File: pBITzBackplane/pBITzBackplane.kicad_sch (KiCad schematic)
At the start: 13 parts

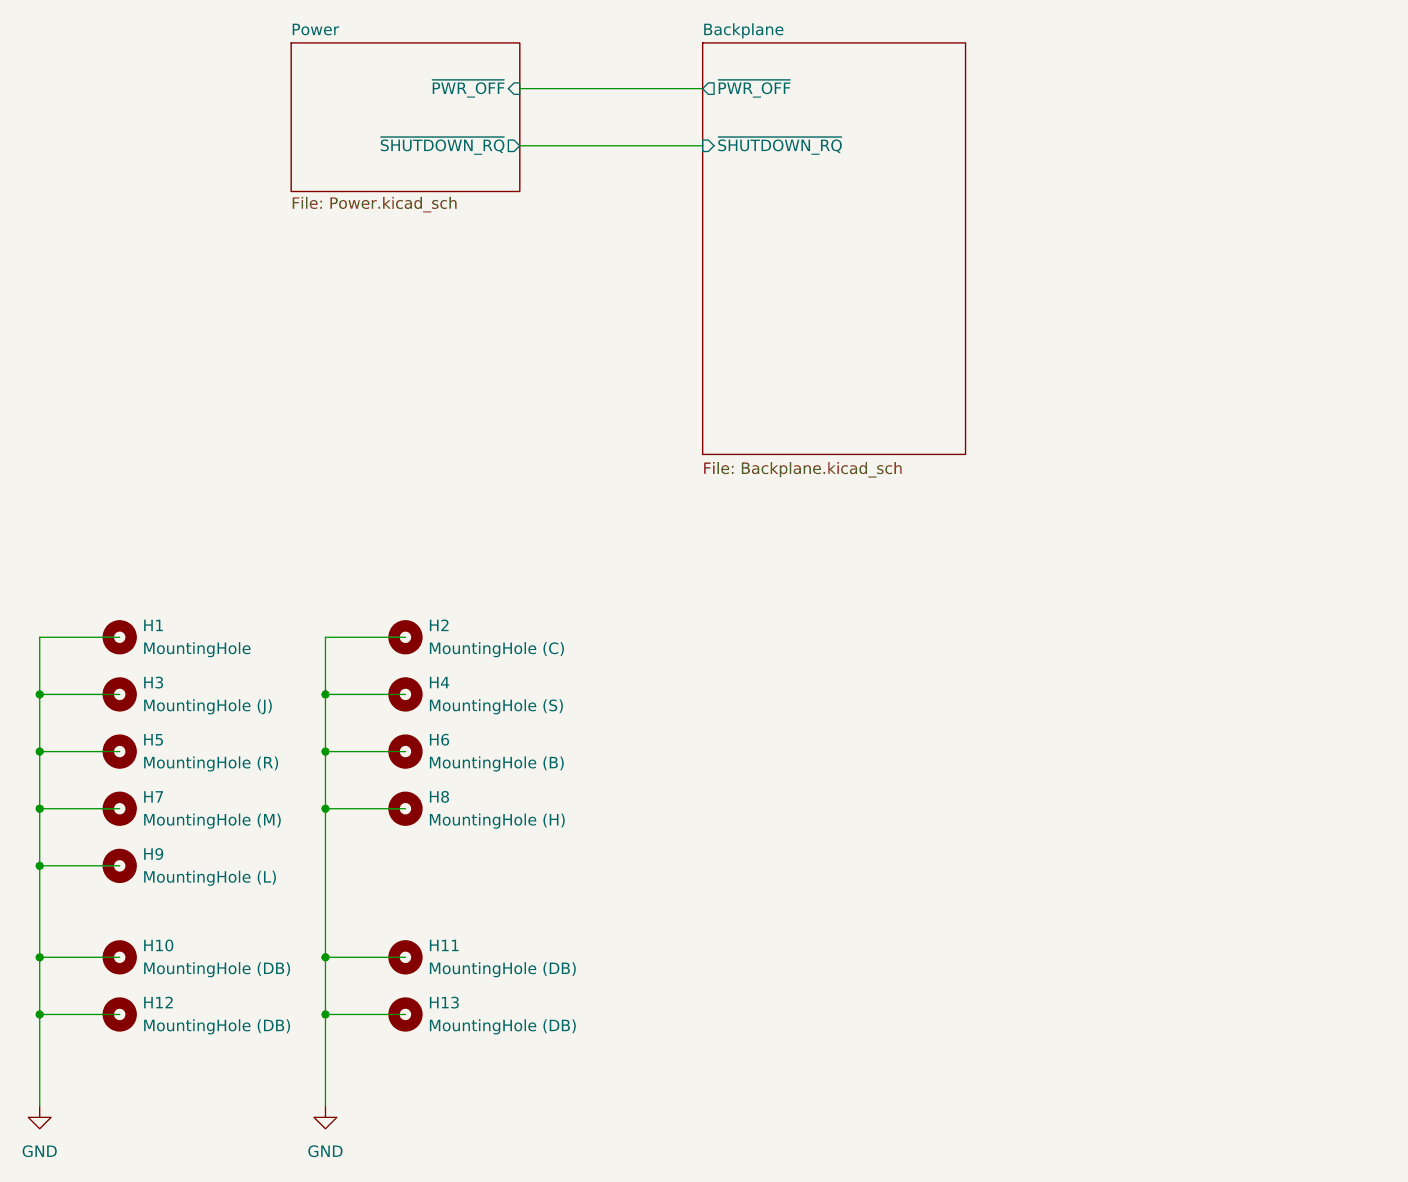
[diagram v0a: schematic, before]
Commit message: Changed the pBITz backplane connector from a PCIe 8x to a DIN 41612 connector.
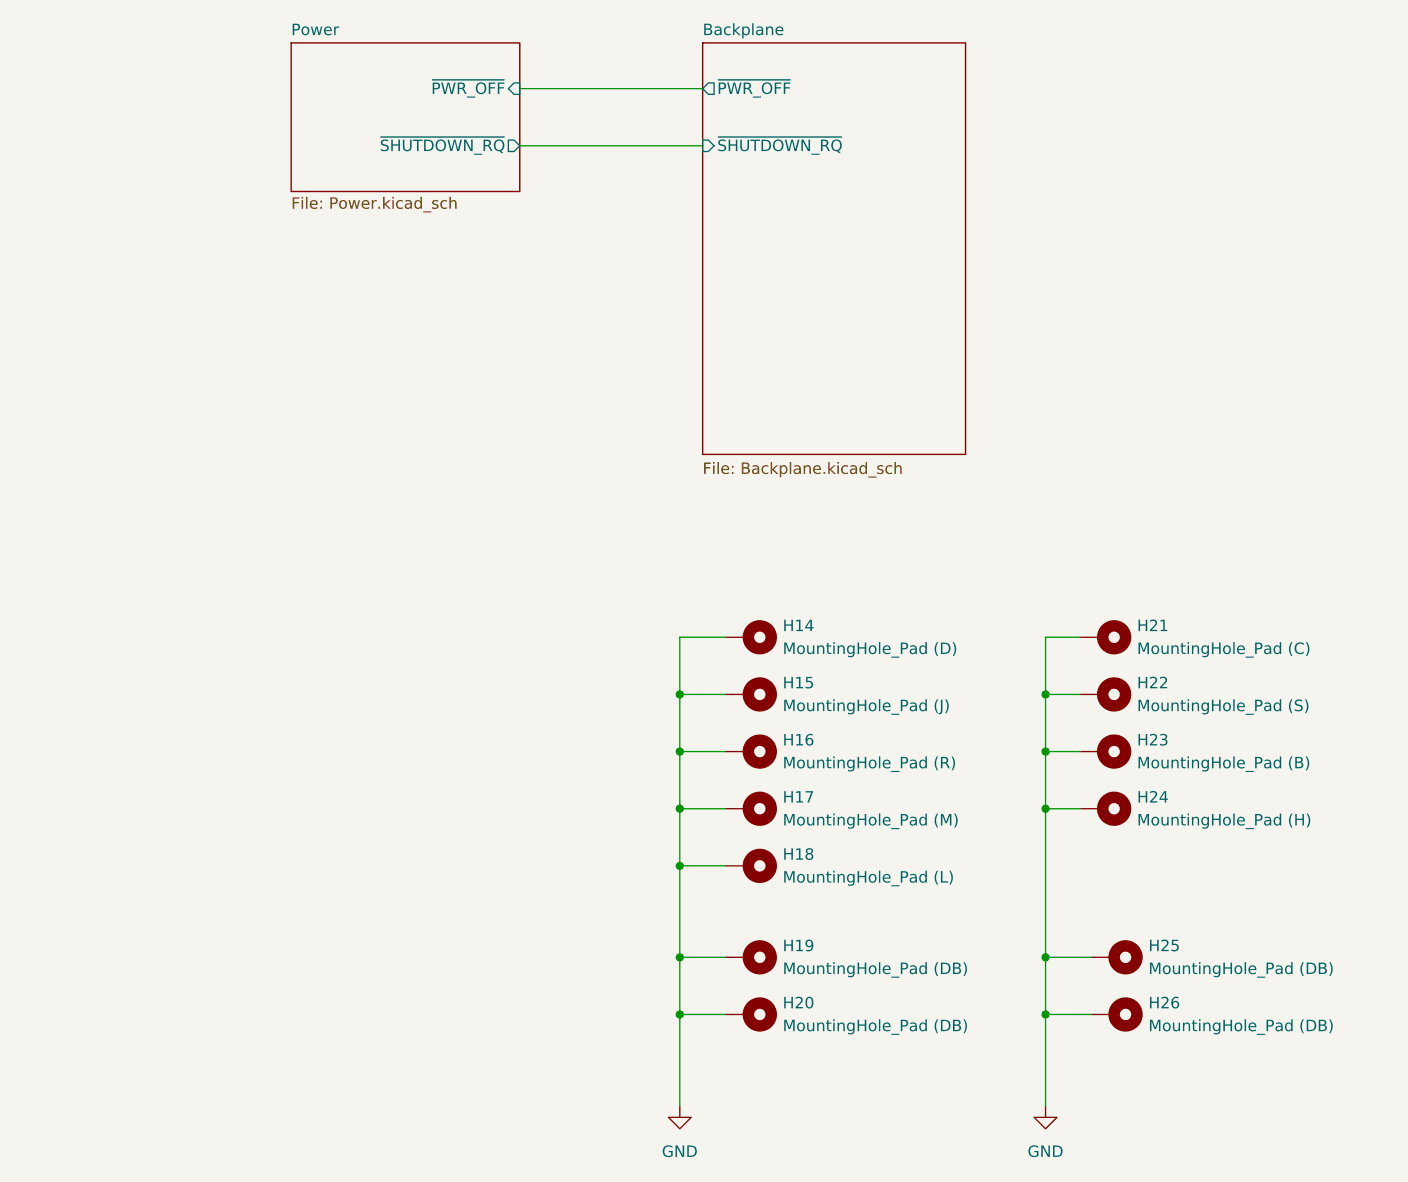
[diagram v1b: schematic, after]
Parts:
- removed H1: MountingHole, MountingHole:MountingHole_3.5mm_Pad_TopBottom, symbol Mechanical:MountingHole
- removed H10, H11, H12, H13: MountingHole (DB), MountingHole:MountingHole_3.5mm_Pad_TopBottom, symbol Mechanical:MountingHole
- removed H2: MountingHole (C), MountingHole:MountingHole_3.5mm_Pad_TopBottom, symbol Mechanical:MountingHole
- removed H3: MountingHole (J), MountingHole:MountingHole_3.5mm_Pad_TopBottom, symbol Mechanical:MountingHole
- removed H4: MountingHole (S), MountingHole:MountingHole_3.5mm_Pad_TopBottom, symbol Mechanical:MountingHole
- removed H5: MountingHole (R), MountingHole:MountingHole_3.5mm_Pad_TopBottom, symbol Mechanical:MountingHole
- removed H6: MountingHole (B), MountingHole:MountingHole_3.5mm_Pad_TopBottom, symbol Mechanical:MountingHole
- removed H7: MountingHole (M), MountingHole:MountingHole_3.5mm_Pad_TopBottom, symbol Mechanical:MountingHole
- removed H8: MountingHole (H), MountingHole:MountingHole_3.5mm_Pad_TopBottom, symbol Mechanical:MountingHole
- removed H9: MountingHole (L), MountingHole:MountingHole_3.5mm_Pad_TopBottom, symbol Mechanical:MountingHole
- added H14: MountingHole_Pad (D), MountingHole:MountingHole_3.5mm_Pad_TopBottom, symbol Mechanical:MountingHole_Pad
- added H15: MountingHole_Pad (J), MountingHole:MountingHole_3.5mm_Pad_TopBottom, symbol Mechanical:MountingHole_Pad
- added H16: MountingHole_Pad (R), MountingHole:MountingHole_3.5mm_Pad_TopBottom, symbol Mechanical:MountingHole_Pad
- added H17: MountingHole_Pad (M), MountingHole:MountingHole_3.5mm_Pad_TopBottom, symbol Mechanical:MountingHole_Pad
- added H18: MountingHole_Pad (L), MountingHole:MountingHole_3.5mm_Pad_TopBottom, symbol Mechanical:MountingHole_Pad
- added H19, H20, H25, H26: MountingHole_Pad (DB), MountingHole:MountingHole_3.5mm_Pad_TopBottom, symbol Mechanical:MountingHole_Pad
- added H21: MountingHole_Pad (C), MountingHole:MountingHole_3.5mm_Pad_TopBottom, symbol Mechanical:MountingHole_Pad
- added H22: MountingHole_Pad (S), MountingHole:MountingHole_3.5mm_Pad_TopBottom, symbol Mechanical:MountingHole_Pad
- added H23: MountingHole_Pad (B), MountingHole:MountingHole_3.5mm_Pad_TopBottom, symbol Mechanical:MountingHole_Pad
- added H24: MountingHole_Pad (H), MountingHole:MountingHole_3.5mm_Pad_TopBottom, symbol Mechanical:MountingHole_Pad
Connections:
- net GND: now also H14.1, H15.1, H16.1, H17.1, H18.1, H19.1, H20.1, H21.1, H22.1, H23.1, H24.1, H25.1, H26.1
